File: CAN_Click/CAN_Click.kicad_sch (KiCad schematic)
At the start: 22 parts, among them J1 CAN, J2 CAN Click v${REVISION} by MPro, U1 MCP2515-xST, U2 COS1042T/3, Y1 16MHz

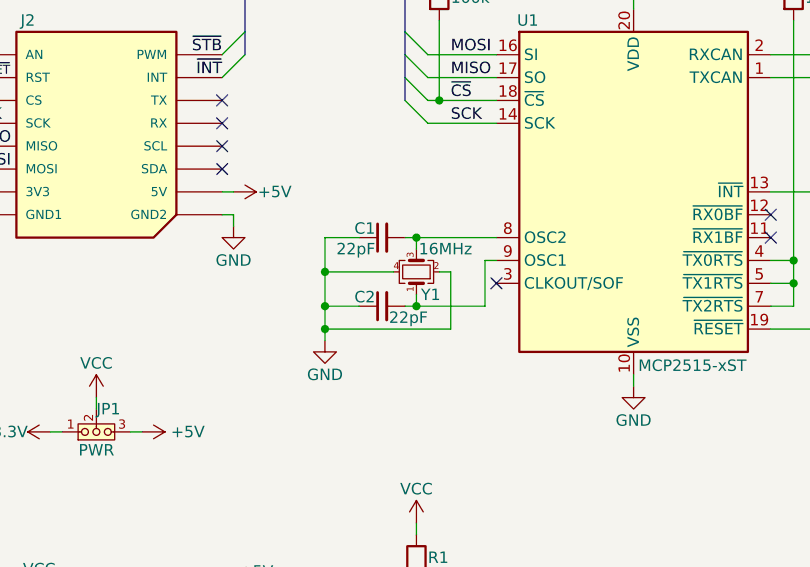
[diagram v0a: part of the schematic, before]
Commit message: quartz changed to 12MHz
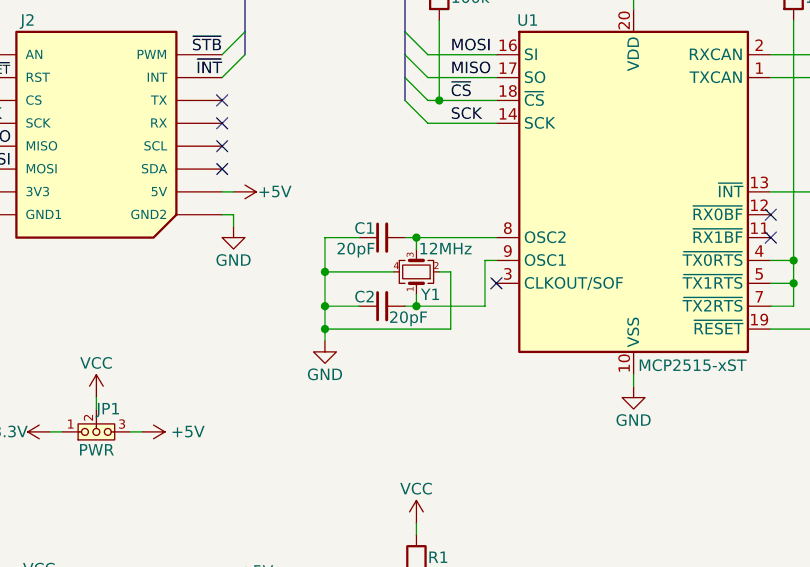
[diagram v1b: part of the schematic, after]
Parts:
- C1, C2: value 22pF -> 20pF; LCSC C1804 -> C1798
- JP1: LCSC ----- -> C5383112
- JP2: LCSC ----- -> C5383111
- Y1: value 16MHz -> 12MHz; LCSC C5380579 -> C9002
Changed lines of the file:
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@@
 			)
 		)
-		(property "LCSC" "-----"
+		(property "LCSC" "C5383112"
 			(at 39.37 88.9 0)
 			(effects
@@
 			)
 		)
-		(property "Value" "16MHz"
+		(property "Value" "12MHz"
 			(at 75.184 68.58 90)
 			(effects
@@
 			)
 		)
-		(property "LCSC" "C5380579"
+		(property "LCSC" "C9002"
 			(at 74.93 71.12 90)
 			(effects
@@
 			)
 		)
-		(property "LCSC" "-----"
+		(property "LCSC" "C5383111"
 			(at 173.99 40.64 90)
 			(effects
@@
 			)
 		)
-		(property "Value" "22pF"
+		(property "Value" "20pF"
 			(at 71.882 76.2 90)
 			(effects
@@
 			)
 		)
-		(property "LCSC" "C1804"
+		(property "LCSC" "C1798"
 			(at 71.12 74.93 90)
 			(effects
@@
 			)
 		)
-		(property "Value" "22pF"
+		(property "Value" "20pF"
 			(at 70.358 68.58 90)
 			(effects
@@
 			)
 		)
-		(property "LCSC" "C1804"
+		(property "LCSC" "C1798"
 			(at 71.12 67.31 90)
 			(effects
